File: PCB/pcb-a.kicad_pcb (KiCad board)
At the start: 2 copper layers, 116.3 x 50.4 mm, 33 parts, among them Q1 BC337, Q2 BC337, Q3 BC337, U1 MCP23008-xP, U4 ATmega16L-8P

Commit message: fixes
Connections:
- U1 pad 14: o_engineOFF -> o_engineON
- to_pcbB2 pad 5: unconnected-(to_pcbB2-Pad5) -> o_engineON
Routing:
- net o_engineON: track 0.00 -> 140.7 mm, vias 0 -> 2
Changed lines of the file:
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@@
   (net 64 "unconnected-(KeyLocker1-Pad5)")
   (net 65 "unconnected-(KeyLocker1-Pad6)")
-  (net 66 "o_engineOFF")
+  (net 66 "o_engineON")
   (net 67 "c_rearLight")
   (net 68 "c_brakeSwitch")
   (net 69 "unconnected-(RearDevs1-Pad4)")
-  (net 70 "unconnected-(to_pcbB2-Pad5)")
-  (net 71 "unconnected-(to_pcbB3-Pad4)")
+  (net 70 "unconnected-(to_pcbB3-Pad4)")
   (footprint "Connector_Wire:SolderWire-0.5sqmm_1x02_P4.6mm_D0.9mm_OD2.1mm" (layer "F.Cu")
     (at 194.572 59.324 180)
@@
       (net 42 "i_startButton") (pinfunction "GP3") (pintype "bidirectional"))
     (pad "14" thru_hole oval (at 7.62 10.16 180) (size 1.6 1.6) (drill 0.8) (layers *.Cu *.Mask)
-      (net 66 "o_engineOFF") (pinfunction "GP4") (pintype "bidirectional"))
+      (net 66 "o_engineON") (pinfunction "GP4") (pintype "bidirectional"))
     (pad "15" thru_hole oval (at 7.62 7.62 180) (size 1.6 1.6) (drill 0.8) (layers *.Cu *.Mask)
       (net 56 "i_neutral") (pinfunction "GP5") (pintype "bidirectional"))
@@
       (net 63 "c_engineOFF") (pinfunction "Pin_4") (pintype "passive"))
     (pad "5" thru_hole oval (at 0 10.16 90) (size 1.7 1.7) (drill 1) (layers *.Cu *.Mask)
-      (net 70 "unconnected-(to_pcbB2-Pad5)") (pinfunction "Pin_5") (pintype "passive+no_connect"))
+      (net 66 "o_engineON") (pinfunction "Pin_5") (pintype "passive"))
     (model "${KICAD6_3DMODEL_DIR}/Connector_PinHeader_2.54mm.3dshapes/PinHeader_1x05_P2.54mm_Vertical.wrl"
       (offset (xyz 0 0 0))
@@
       (net 23 "o_neutral") (pinfunction "Pin_3") (pintype "passive"))
     (pad "4" thru_hole oval (at 0 7.62 270) (size 1.7 1.7) (drill 1) (layers *.Cu *.Mask)
-      (net 71 "unconnected-(to_pcbB3-Pad4)") (pinfunction "Pin_4") (pintype "passive+no_connect"))
+      (net 70 "unconnected-(to_pcbB3-Pad4)") (pinfunction "Pin_4") (pintype "passive+no_connect"))
     (pad "5" thru_hole oval (at 0 10.16 270) (size 1.7 1.7) (drill 1) (layers *.Cu *.Mask)
       (net 3 "c_leftArrow") (pinfunction "Pin_5") (pintype "passive"))
@@
   (segment (start 198.636 105.298) (end 159.012 105.298) (width 0.5) (layer "B.Cu") (net 63))
   (segment (start 143.777 90.566) (end 143.777 91.841) (width 0.5) (layer "B.Cu") (net 63))
+  (segment (start 157.996 103.52) (end 160.474 105.998) (width 0.5) (layer "F.Cu") (net 66))
+  (segment (start 203.208 101.715949) (end 203.208 97.17) (width 0.5) (layer "F.Cu") (net 66))
+  (segment (start 203.208 97.17) (end 206.51 93.868) (width 0.5) (layer "F.Cu") (net 66))
+  (segment (start 154.948 99.202) (end 157.996 102.25) (width 0.5) (layer "F.Cu") (net 66))
+  (segment (start 206.51 93.868) (end 206.51 68.722) (width 0.5) (layer "F.Cu") (net 66))
+  (segment (start 160.474 105.998) (end 198.92595 105.998) (width 0.5) (layer "F.Cu") (net 66))
+  (segment (start 198.92595 105.998) (end 203.208 101.715949) (width 0.5) (layer "F.Cu") (net 66))
+  (segment (start 206.51 68.722) (end 199.398 61.61) (width 0.5) (layer "F.Cu") (net 66))
+  (segment (start 199.398 61.61) (end 186.444 61.61) (width 0.5) (layer "F.Cu") (net 66))
+  (segment (start 157.996 102.25) (end 157.996 103.52) (width 0.5) (layer "F.Cu") (net 66))
+  (via (at 154.948 99.202) (size 0.8) (drill 0.4) (layers "F.Cu" "B.Cu") (net 66))
+  (via (at 186.444 61.61) (size 0.8) (drill 0.4) (layers "F.Cu" "B.Cu") (net 66))
+  (segment (start 186.444 61.61) (end 186.444 73.802) (width 0.5) (layer "B.Cu") (net 66))
+  (segment (start 146.317 90.566) (end 154.948 99.197) (width 0.5) (layer "B.Cu") (net 66))
+  (segment (start 154.948 99.197) (end 154.948 99.202) (width 0.5) (layer "B.Cu") (net 66))
+  (segment (start 186.444 73.802) (end 190.244 77.602) (width 0.5) (layer "B.Cu") (net 66))
   (segment (start 133.358 89.55) (end 129.802 85.994) (width 0.5) (layer "F.Cu") (net 67))
   (segment (start 131.58 83.708) (end 133.104 82.184) (width 0.5) (layer "F.Cu") (net 67))

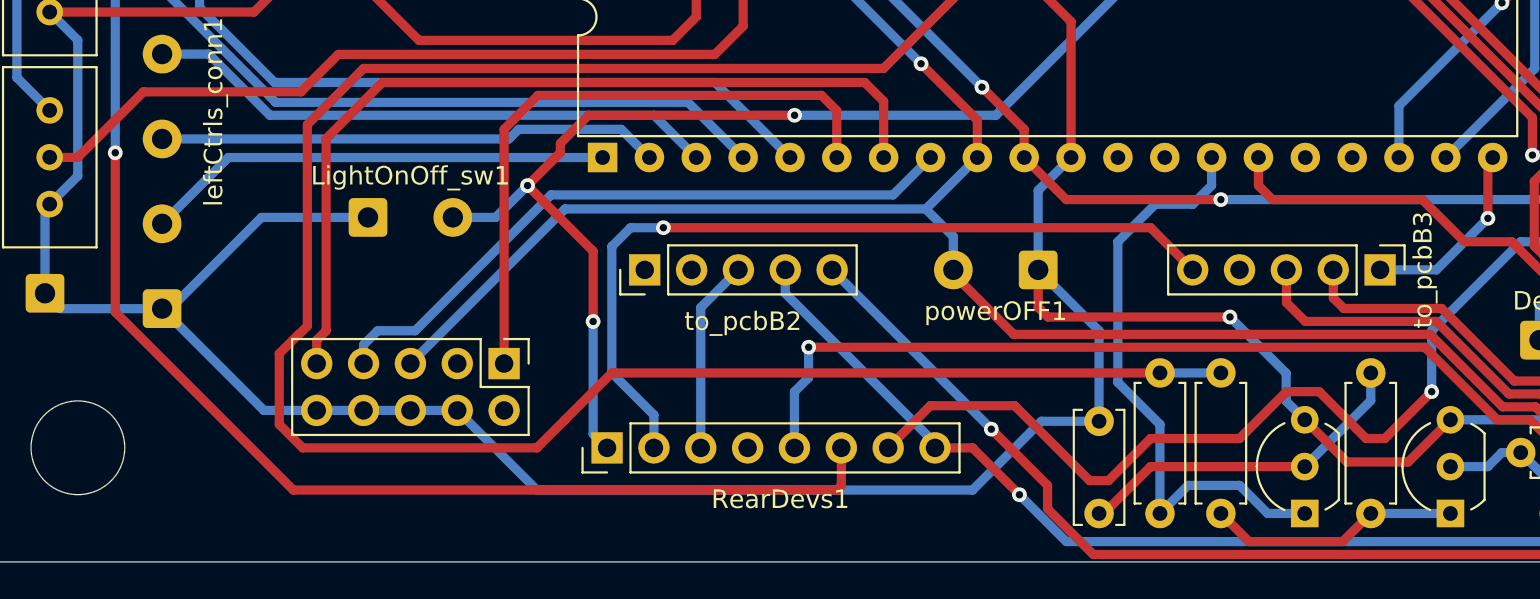
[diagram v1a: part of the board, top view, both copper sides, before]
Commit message: SPI-port activities led added
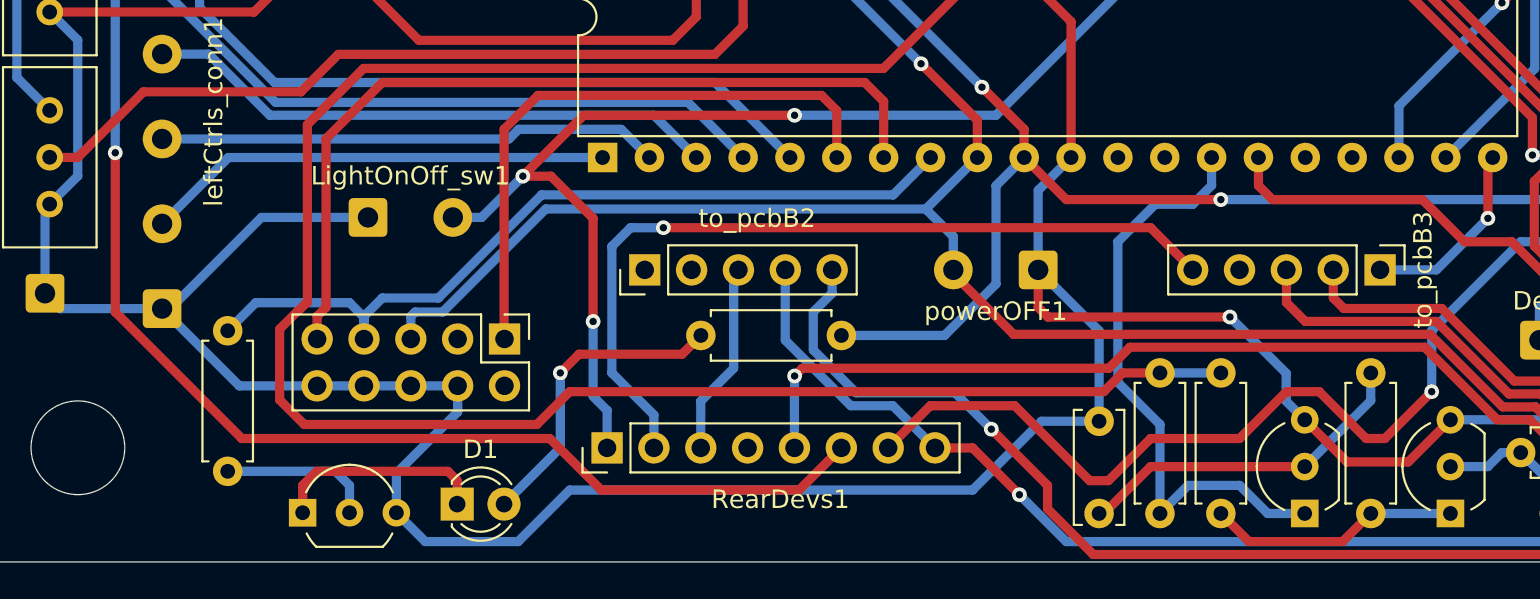
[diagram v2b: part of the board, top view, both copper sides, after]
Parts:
- added D1: LED, LED_THT:LED_D3.0mm, F.Cu at (126.0, 103.3)
- added Q4: BC337, Package_TO_SOT_THT:TO-92_Inline_Wide, F.Cu at (117.6, 103.7)
- added R8: 10K, Resistor_THT:R_Axial_DIN0207_L6.3mm_D2.5mm_P7.62mm_Horizontal, F.Cu at (113.5, 101.5)
- added R9: 5K, Resistor_THT:R_Axial_DIN0207_L6.3mm_D2.5mm_P7.62mm_Horizontal, F.Cu at (139.2, 94.1)
- moved ISP101 1.33 mm to (128.6, 94.3)
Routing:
- net tempPower: track 90.6 -> 107.6 mm
- net Net-(D1-Pad2): track 0.00 -> 16.8 mm, vias 0 -> 1
- net Net-(D1-Pad1): track 0.00 -> 11.7 mm
- net GND: track 284.0 -> 295.0 mm
- net Net-(ISP101-Pad7): track 36.0 -> 45.0 mm
- net Net-(Q4-Pad2): track 0.00 -> 8.40 mm
- net o_engineON: track 140.7 -> 144.7 mm
- net +5V: track 191.0 -> 189.1 mm
- net Net-(ISP101-Pad9): track 47.4 -> 46.0 mm
- net c_engineOFF: track 95.2 -> 96.6 mm
- net Net-(ISP101-Pad1): track 34.4 -> 33.1 mm
- net c_rearLight: track 63.7 -> 65.0 mm
- net c_startEngine: track 85.5 -> 84.3 mm

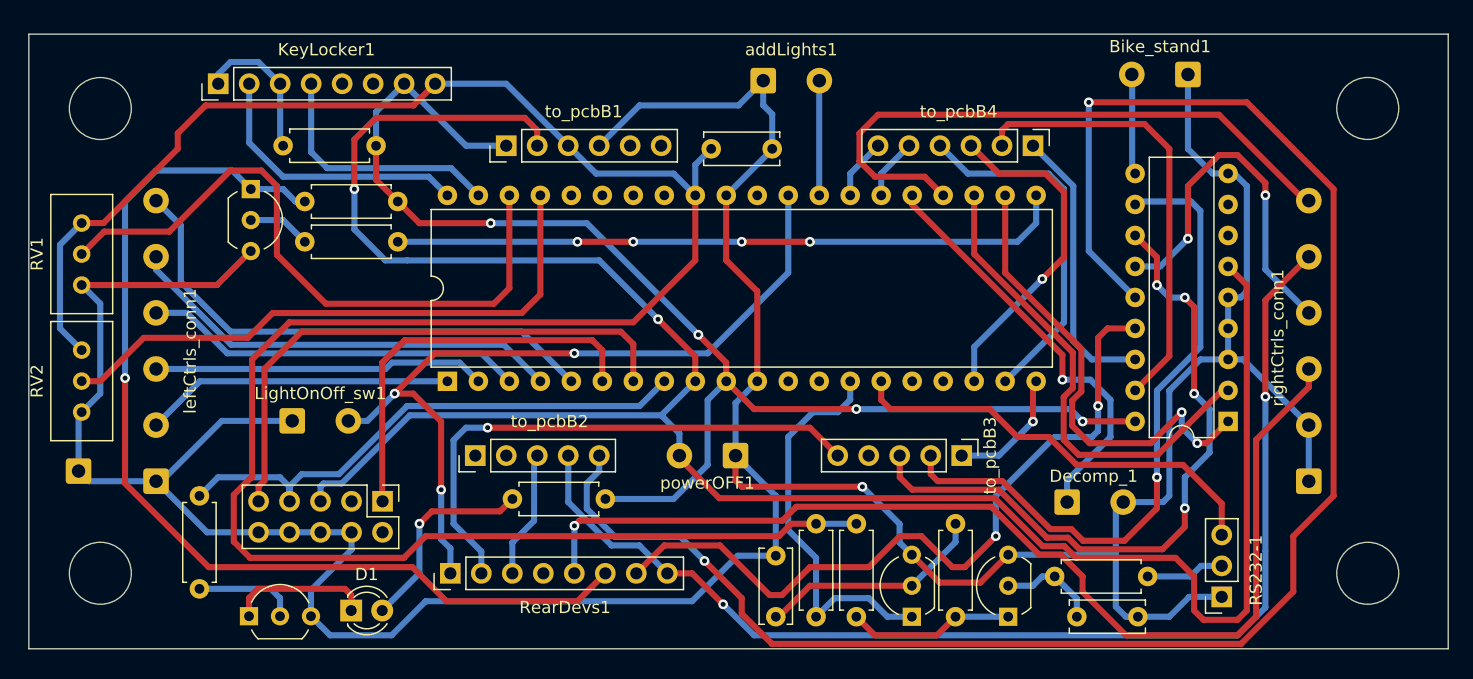
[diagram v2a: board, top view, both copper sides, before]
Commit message: Configuration dip-switches added and partial PCB refactoring
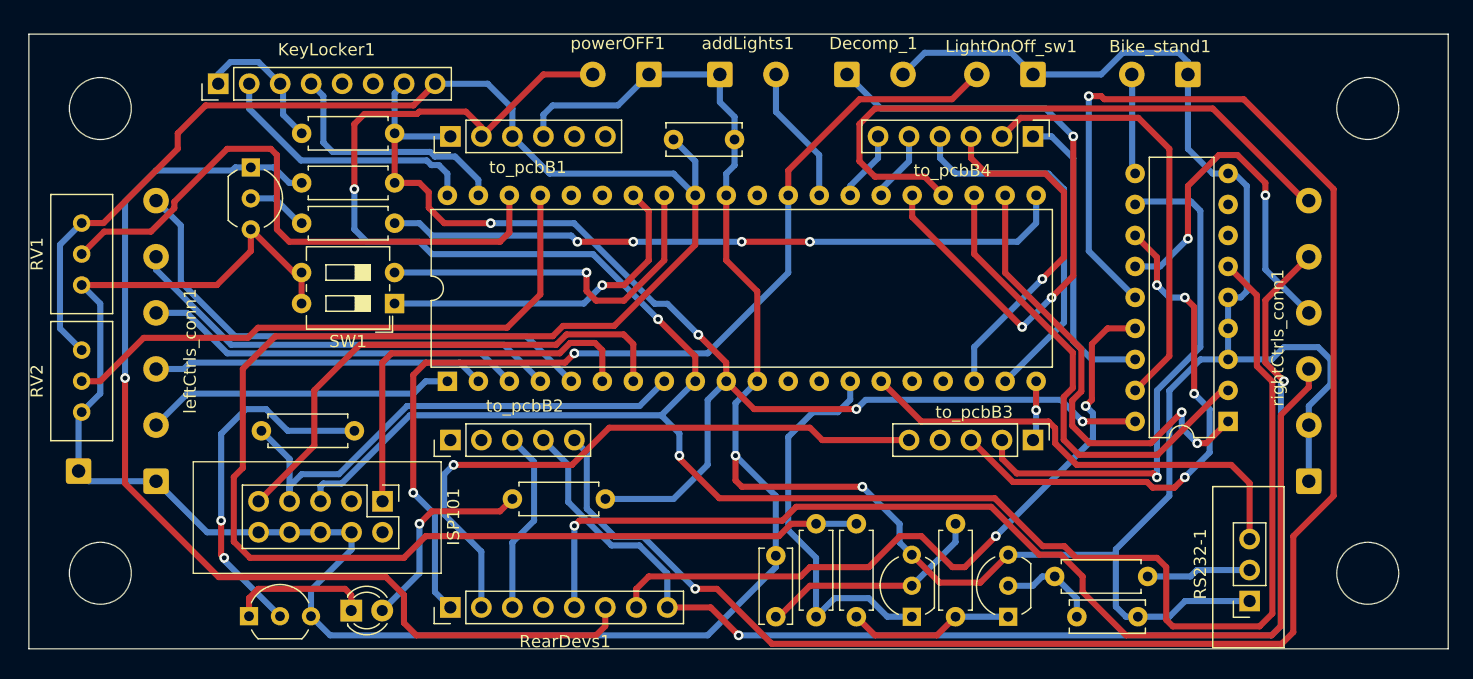
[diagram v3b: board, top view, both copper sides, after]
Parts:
- added SW1: SW_DIP_x02, Button_Switch_THT:SW_DIP_SPSTx02_Slide_6.7x6.64mm_W7.62mm_P2.54mm_LowProfile, F.Cu at (129.5, 78.1)
- moved LightOnOff_sw1 67.0 mm to (181.9, 59.3), turned to 180 degrees
- moved Decomp_1 39.4 mm to (166.6, 59.3)
- moved powerOFF1 32.0 mm to (150.4, 59.3)
- moved R8 18.1 mm to (126.2, 88.5), turned to 180 degrees
- moved to_pcbB3 5.98 mm to (181.9, 89.3)
- moved to_pcbB1 4.64 mm to (134.1, 64.4)
- moved addLights1 3.59 mm to (156.2, 59.3)
- moved C2 3.18 mm to (152.4, 64.7)
- moved RearDevs1 2.79 mm to (134.1, 103.0)
- moved to_pcbB2 2.40 mm to (134.1, 89.3)
- moved RS232-1 2.31 mm to (199.6, 102.5)
- moved R1 1.83 mm to (129.5, 64.2)
- moved Q3 1.78 mm to (117.8, 66.9)
- moved R6 1.55 mm to (121.9, 68.2)
- moved R7 1.55 mm to (121.9, 71.5)
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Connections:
- U4 pad 33: unconnected-(U4-Pad33) -> Net-(SW1-Pad2)
- U4 pad 34: unconnected-(U4-Pad34) -> Net-(SW1-Pad1)
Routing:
- net GND: track 295.0 -> 327.6 mm, vias 1 -> 2
- net Net-(SW1-Pad2): track 0.00 -> 30.7 mm, vias 0 -> 1
- net Net-(SW1-Pad1): track 0.00 -> 28.2 mm, vias 0 -> 1
- net Net-(Q4-Pad2): track 8.40 -> 29.4 mm, vias 0 -> 2
- net i_decompr: track 34.7 -> 52.5 mm, vias 1 -> 3
- net c_rearLight: track 65.0 -> 81.6 mm, vias 3 -> 2
- net o_neutral: track 56.4 -> 43.4 mm
- net i_powerOFF: track 181.5 -> 193.2 mm, vias 2 -> 3
- net o_engineReady: track 55.0 -> 43.9 mm
- net c_leftArrow: track 44.7 -> 52.3 mm
- net c_engineOFF: track 96.6 -> 103.3 mm
- net tempPower: track 107.6 -> 101.2 mm
- net o_keepAlive: track 10.4 -> 4.93 mm
- net Net-(RV1-Pad2): track 53.9 -> 49.0 mm
- net c_rightArrow: track 10.5 -> 15.2 mm
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
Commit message: fixes
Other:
- outline, holes or cut-outs redrawn
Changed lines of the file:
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@@
   (gr_rect (start 196.604 93.106) (end 202.446 106.314) (layer "F.SilkS") (width 0.12) (fill none))
   (gr_rect (start 113.038 91.074) (end 133.358 100.218) (layer "F.SilkS") (width 0.1) (fill none))
-  (gr_circle (center 209.309589 62.112478) (end 211.849589 62.112478) (layer "Edge.Cuts") (width 0.05) (fill none))
-  (gr_circle (center 209.309589 100.212478) (end 211.849589 100.212478) (layer "Edge.Cuts") (width 0.05) (fill none))
-  (gr_circle (center 105.423589 100.212478) (end 107.963589 100.212478) (layer "Edge.Cuts") (width 0.05) (fill none))
-  (gr_circle (center 105.423589 62.118) (end 107.963589 62.118) (layer "Edge.Cuts") (width 0.05) (fill none))
+  (gr_circle (center 105.682866 62.118) (end 107.963522 61.869522) (layer "Edge.Cuts") (width 0.05) (fill none))
+  (gr_circle (center 209.817344 62.118) (end 212.098 61.869522) (layer "Edge.Cuts") (width 0.05) (fill none))
+  (gr_circle (center 209.817344 100.212478) (end 212.098 99.964) (layer "Edge.Cuts") (width 0.05) (fill none))
+  (gr_circle (center 105.663849 100.212478) (end 107.944505 99.964) (layer "Edge.Cuts") (width 0.05) (fill none))
   (gr_rect (start 99.565 56.022) (end 215.908 106.402) (layer "Edge.Cuts") (width 0.05) (fill none))
-  (gr_circle (center 105.672 100.212478) (end 111.514 100.466545) (layer "Margin") (width 0.1) (fill none))
-  (gr_circle (center 105.672 62.118) (end 111.514 62.372067) (layer "Margin") (width 0.1) (fill none))
-  (gr_circle (center 209.558 100.212478) (end 215.4 100.466545) (layer "Margin") (width 0.1) (fill none))
-  (gr_circle (center 209.558 62.112478) (end 215.4 62.366545) (layer "Margin") (width 0.1) (fill none))
+  (gr_circle (center 209.812 100.212478) (end 215.654 100.466545) (layer "Margin") (width 0.1) (fill none))
+  (gr_circle (center 105.658505 100.212478) (end 111.500505 100.466545) (layer "Margin") (width 0.1) (fill none))
+  (gr_circle (center 105.677522 62.118) (end 111.519522 62.372067) (layer "Margin") (width 0.1) (fill none))
+  (gr_circle (center 209.812 62.118) (end 215.654 62.372067) (layer "Margin") (width 0.1) (fill none))
   (dimension (type aligned) (layer "B.Mask")
-    (pts (xy 99.576 55.68) (xy 216.427 55.68))
+    (pts (xy 99.565 56.022) (xy 215.908 56.022))
     (height -4.738)
-    (gr_text "116,8510 mm" (at 158.0015 49.792) (layer "B.Mask")
+    (gr_text "116,3430 mm" (at 157.7365 50.134) (layer "B.Mask")
       (effects (font (size 1 1) (thickness 0.15)))
     )
@@
   )
   (dimension (type aligned) (layer "B.Mask")
-    (pts (xy 105.423589 62.118) (xy 105.423589 100.212478))
+    (pts (xy 105.682866 62.118) (xy 105.663849 100.212478))
     (height 9.657589)
-    (gr_text "38,0945 mm" (at 94.616 81.165239 90) (layer "B.Mask")
+    (gr_text "38,0945 mm" (at 94.86577 81.159844 89.9713991) (layer "B.Mask")
       (effects (font (size 1 1) (thickness 0.15)))
     )
@@
   )
   (dimension (type aligned) (layer "B.Mask")
-    (pts (xy 105.423589 100.212478) (xy 209.309589 100.212478))
+    (pts (xy 105.658505 100.212478) (xy 209.812 100.212478))
     (height 10.927522)
-    (gr_text "103,8860 mm" (at 157.366589 109.99) (layer "B.Mask")
+    (gr_text "104,1535 mm" (at 157.735252 109.99) (layer "B.Mask")
       (effects (font (size 1 1) (thickness 0.15)))
     )
@@
   (segment (start 117.61 103.732) (end 117.61 102.25) (width 0.5) (layer "F.Cu") (net 73))
   (segment (start 125.484 101.488) (end 125.987 101.991) (width 0.5) (layer "F.Cu") (net 73))
-  (group "" (id 01a48bd9-2a0e-4b43-82a9-cdb8d78936d6)
+  (group "" (id 1191cbb4-e868-45f0-9b39-0c9024056cfc)
     (members
-      05553d34-2925-4bdc-8bab-f9f5b3c55f82
-      98c1bbca-1fff-4140-9564-036468572850
-    )
-  )
-  (group "" (id 253c07d0-8b56-443c-8c68-2271fb73760d)
+      1ea9ef13-f563-41d1-a8f6-1e2cb00ccbf7
+      9438a5aa-eef2-4593-ab90-e2163a57d33e
+    )
+  )
+  (group "" (id 238341a2-c60a-4837-b744-5691eaa33d93)
+    (members
+      3010c1c4-469c-4354-abc8-53d22652e3ed
+      c45d402f-1a26-4fe2-8344-1050baa32279
+    )
+  )
+  (group "" (id 9d6b8b74-bb01-4229-a181-a39289eb290b)
     (members
       198ffc1c-39e1-4c4c-8a2d-9dd88408dbde
@@
     )
   )
-  (group "" (id 61a310f2-1cb2-413c-8545-ec5ad506d193)
+  (group "" (id dbfaaa01-c9ae-441e-87c0-ab444ec25e89)
     (members
-      14dd9be3-aed6-412b-97ca-53051d9353e5
-      d13d56c9-9469-4be9-b6a0-277f87dc44ae
-    )
-  )
-  (group "" (id d2ff0935-d21d-40ba-8411-cf09b2b1f453)
-    (members
-      0f17db16-33e6-4476-b6db-e9f8db459e64
-      c424aa93-48f7-4c7a-98ff-3443ed3fcc41
-    )
-  )
+      35c22e0c-a422-413e-b740-b398cd6d7ad2
+      db7f76ad-4333-4102-9a41-cba291edbf3f
+    )
+  )
